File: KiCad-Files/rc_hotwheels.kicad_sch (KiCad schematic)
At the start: 9 parts, among them IC1 BD6211F-E2, IC2 MIC5504-3.3YM5-TR, U1 STM32F070F6P6, U3 NRF24L01_Breakout

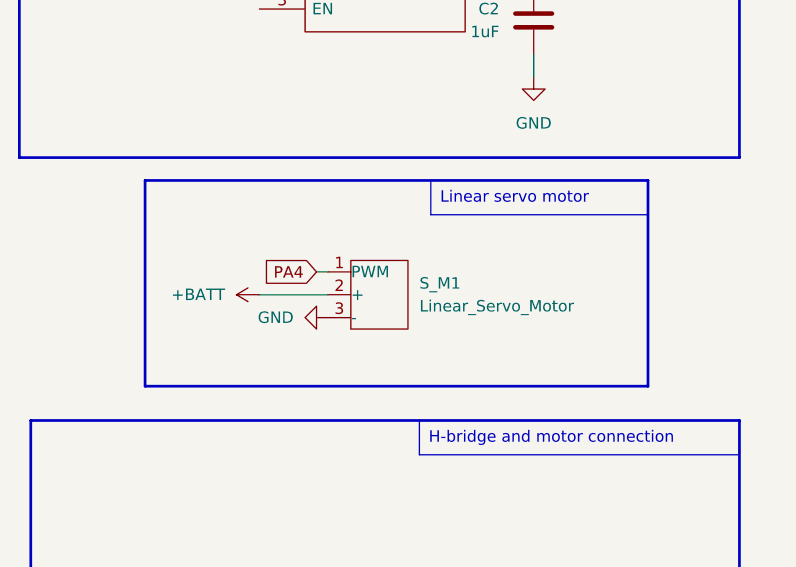
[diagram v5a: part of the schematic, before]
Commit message: Servo motor connection
Deleted unused component - servo motor, instead used mounting holes
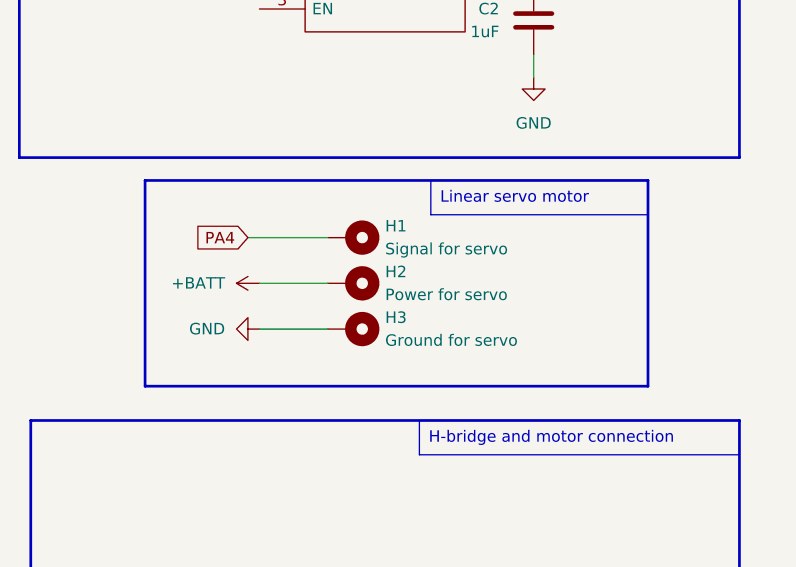
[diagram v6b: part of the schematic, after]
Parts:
- removed S_M1: Linear_Servo_Motor, symbol Motor:Motor_Servo
- added H1: Signal for servo, symbol Mechanical:MountingHole_Pad
- added H2: Power for servo, symbol Mechanical:MountingHole_Pad
- added H3: Ground for servo, symbol Mechanical:MountingHole_Pad
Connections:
- net +BATT: now also H2.1
- net GND: now also H3.1
- net PA4: now also H1.1
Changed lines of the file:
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@@
+    (stroke (width 0) (type default))
+  )
+  (wire (pts (xy 41.91 128.27) (xy 49.53 128.27))
     (stroke (width 0) (type default))
   )
@@
     (stroke (width 0) (type default))
   )
-  (wire (pts (xy 41.91 124.46) (xy 49.53 124.46))
+  (wire (pts (xy 41.91 123.19) (xy 49.53 123.19))
     (stroke (width 0) (type default))
   )
@@
     (stroke (width 0) (type default))
   )
-  (wire (pts (xy 48.26 121.92) (xy 49.53 121.92))
+  (wire (pts (xy 40.64 118.11) (xy 49.53 118.11))
     (stroke (width 0) (type default))
   )
@@
     )
   )
-  (global_label "PA4" (shape input) (at 48.26 121.92 180) (fields_autoplaced)
-    (effects (font (size 1.27 1.27)) (justify right))
-    (property "Intersheetrefs" "${INTERSHEET_REFS}" (at 41.7067 121.92 0)
-      (effects (font (size 1.27 1.27)) (justify right) hide)
-    )
-    (property "Servo Control" "" (at 48.26 124.1108 0)
+  (global_label "PA4" (shape input) (at 40.64 118.11 180) (fields_autoplaced)
+    (effects (font (size 1.27 1.27)) (justify right))
+    (property "Intersheetrefs" "${INTERSHEET_REFS}" (at 34.0867 118.11 0)
+      (effects (font (size 1.27 1.27)) (justify right) hide)
+    )
+    (property "Servo Control" "" (at 40.64 120.3008 0)
       (effects (font (size 1.27 1.27)) (justify right) hide)
     )
@@
     (property "Intersheetrefs" "${INTERSHEET_REFS}" (at 87.41 90.17 0)
       (effects (font (size 1.27 1.27)) (justify left) hide)
+    )
+  )
+  (symbol (lib_id "Mechanical:MountingHole_Pad") (at 52.07 118.11 270) (unit 1)
+    (in_bom yes) (on_board yes) (dnp no) (fields_autoplaced)
+    (property "Reference" "H1" (at 55.88 116.84 90)
+      (effects (font (size 1.27 1.27)) (justify left))
+    )
+    (property "Value" "Signal for servo" (at 55.88 119.38 90)
+      (effects (font (size 1.27 1.27)) (justify left))
+    )
+    (property "Footprint" "" (at 52.07 118.11 0)
+      (effects (font (size 1.27 1.27)) hide)
+    )
+    (property "Datasheet" "~" (at 52.07 118.11 0)
+      (effects (font (size 1.27 1.27)) hide)
+    )
+    (pin "1")
+    (instances
+      (project "rc_hotwheels"
+        (path "/0b835094-f9c0-45ab-a312-d1f27d043c8e"
+          (reference "H1") (unit 1)
+        )
+      )
     )
   )
@@
         (path "/0b835094-f9c0-45ab-a312-d1f27d043c8e"
           (reference "#PWR06") (unit 1)
+        )
+      )
+    )
+  )
+  (symbol (lib_id "Mechanical:MountingHole_Pad") (at 52.07 128.27 270) (unit 1)
+    (in_bom yes) (on_board yes) (dnp no) (fields_autoplaced)
+    (property "Reference" "H3" (at 55.88 127 90)
+      (effects (font (size 1.27 1.27)) (justify left))
+    )
+    (property "Value" "Ground for servo" (at 55.88 129.54 90)
+      (effects (font (size 1.27 1.27)) (justify left))
+    )
+    (property "Footprint" "" (at 52.07 128.27 0)
+      (effects (font (size 1.27 1.27)) hide)
+    )
+    (property "Datasheet" "~" (at 52.07 128.27 0)
+      (effects (font (size 1.27 1.27)) hide)
+    )
+    (pin "1")
+    (instances
+      (project "rc_hotwheels"
+        (path "/0b835094-f9c0-45ab-a312-d1f27d043c8e"
+          (reference "H3") (unit 1)
         )
       )
@@
     )
   )
-  (symbol (lib_id "power:+BATT") (at 41.91 124.46 90) (unit 1)
+  (symbol (lib_id "power:+BATT") (at 41.91 123.19 90) (unit 1)
     (in_bom yes) (on_board yes) (dnp no)
-    (property "Reference" "#PWR03" (at 45.72 124.46 0)
-      (effects (font (size 1.27 1.27)) hide)
-    )
-    (property "Value" "+BATT" (at 38.1 124.46 90)
-      (effects (font (size 1.27 1.27)) (justify left))
-    )
-    (property "Footprint" "" (at 41.91 124.46 0)
-      (effects (font (size 1.27 1.27)) hide)
-    )
-    (property "Datasheet" "" (at 41.91 124.46 0)
+    (property "Reference" "#PWR03" (at 45.72 123.19 0)
+      (effects (font (size 1.27 1.27)) hide)
+    )
+    (property "Value" "+BATT" (at 38.1 123.19 90)
+      (effects (font (size 1.27 1.27)) (justify left))
+    )
+    (property "Footprint" "" (at 41.91 123.19 0)
+      (effects (font (size 1.27 1.27)) hide)
+    )
+    (property "Datasheet" "" (at 41.91 123.19 0)
       (effects (font (size 1.27 1.27)) hide)
     )
@@
     )
   )
+  (symbol (lib_id "Mechanical:MountingHole_Pad") (at 52.07 123.19 270) (unit 1)
+    (in_bom yes) (on_board yes) (dnp no) (fields_autoplaced)
+    (property "Reference" "H2" (at 55.88 121.92 90)
+      (effects (font (size 1.27 1.27)) (justify left))
+    )
+    (property "Value" "Power for servo" (at 55.88 124.46 90)
+      (effects (font (size 1.27 1.27)) (justify left))
+    )
+    (property "Footprint" "" (at 52.07 123.19 0)
+      (effects (font (size 1.27 1.27)) hide)
+    )
+    (property "Datasheet" "~" (at 52.07 123.19 0)
+      (effects (font (size 1.27 1.27)) hide)
+    )
+    (pin "1")
+    (instances
+      (project "rc_hotwheels"
+        (path "/0b835094-f9c0-45ab-a312-d1f27d043c8e"
+          (reference "H2") (unit 1)
+        )
+      )
+    )
+  )
   (symbol (lib_id "power:GND") (at 73.66 57.15 0) (unit 1)
     (in_bom yes) (on_board yes) (dnp no) (fields_autoplaced)
@@
     )
   )
-  (symbol (lib_id "power:GND") (at 49.53 127 270) (unit 1)
-    (in_bom yes) (on_board yes) (dnp no) (fields_autoplaced)
-    (property "Reference" "#PWR08" (at 43.18 127 0)
-      (effects (font (size 1.27 1.27)) hide)
-    )
-    (property "Value" "GND" (at 45.72 127 90)
-      (effects (font (size 1.27 1.27)) (justify right))
-    )
-    (property "Footprint" "" (at 49.53 127 0)
-      (effects (font (size 1.27 1.27)) hide)
-    )
-    (property "Datasheet" "" (at 49.53 127 0)
+  (symbol (lib_id "power:GND") (at 41.91 128.27 270) (unit 1)
+    (in_bom yes) (on_board yes) (dnp no) (fields_autoplaced)
+    (property "Reference" "#PWR08" (at 35.56 128.27 0)
+      (effects (font (size 1.27 1.27)) hide)
+    )
+    (property "Value" "GND" (at 38.1 128.27 90)
+      (effects (font (size 1.27 1.27)) (justify right))
+    )
+    (property "Footprint" "" (at 41.91 128.27 0)
+      (effects (font (size 1.27 1.27)) hide)
+    )
+    (property "Datasheet" "" (at 41.91 128.27 0)
       (effects (font (size 1.27 1.27)) hide)
     )
@@
         )
       )
-    )
-  )
-  (symbol (lib_id "Motor:Motor_Servo") (at 57.15 125.73 0) (unit 1)
-    (in_bom yes) (on_board yes) (dnp no) (fields_autoplaced)
-    (property "Reference" "S_M1" (at 59.69 123.19 0)
-      (effects (font (size 1.27 1.27)) (justify left))
-    )
-    (property "Value" "Linear_Servo_Motor" (at 59.69 125.73 0)
-      (effects (font (size 1.27 1.27)) (justify left))
-    )
-    (property "Footprint" "" (at 57.15 129.286 0)
-      (effects (font (size 1.27 1.27)) hide)
-    )
-    (property "Datasheet" "" (at 57.15 129.286 0)
-      (effects (font (size 1.27 1.27)) hide)
-    )
-    (pin "1")
-    (pin "2")
-    (pin "3")
-    (instances
-      (project "rc_hotwheels"
-        (path "/0b835094-f9c0-45ab-a312-d1f27d043c8e"
-          (reference "S_M1") (unit 1)
-        )
-      )

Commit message: Mounting holes footprints added
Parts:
- H1, H2, H3: footprint (none) -> MountingHole:MountingHole_2.2mm_M2_DIN965_Pad
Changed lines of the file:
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@@
       (effects (font (size 1.27 1.27)) (justify left))
     )
-    (property "Footprint" "" (at 52.07 118.11 0)
+    (property "Footprint" "MountingHole:MountingHole_2.2mm_M2_DIN965_Pad" (at 52.07 118.11 0)
       (effects (font (size 1.27 1.27)) hide)
     )
@@
       (effects (font (size 1.27 1.27)) (justify left))
     )
-    (property "Footprint" "" (at 52.07 128.27 0)
+    (property "Footprint" "MountingHole:MountingHole_2.2mm_M2_DIN965_Pad" (at 52.07 128.27 0)
       (effects (font (size 1.27 1.27)) hide)
     )
@@
       (effects (font (size 1.27 1.27)) (justify left))
     )
-    (property "Footprint" "" (at 52.07 123.19 0)
-      (effects (font (size 1.27 1.27)) hide)
-    )
+    (property "Footprint" "MountingHole:MountingHole_2.2mm_M2_DIN965_Pad" (at 52.07 123.19 0)
+      (effects (font (size 1.27 1.27)) hide)
+    )

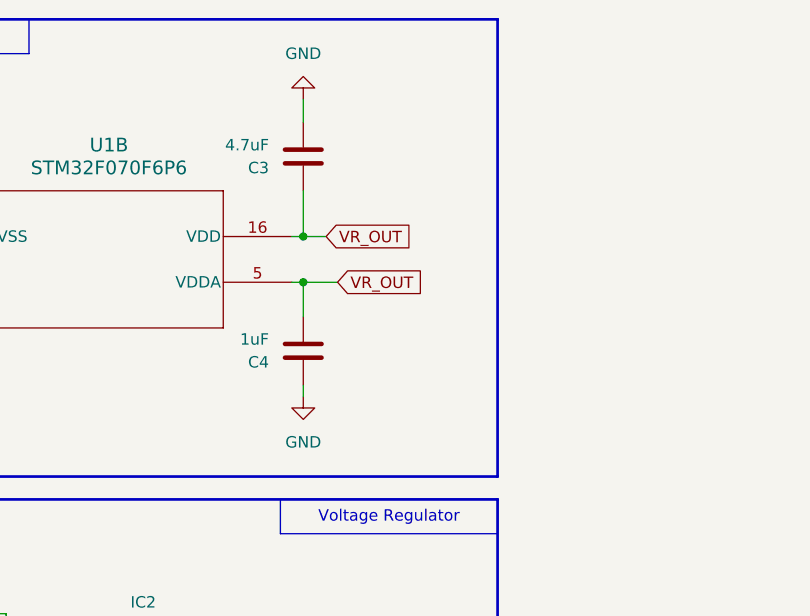
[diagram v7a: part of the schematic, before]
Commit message: Added more capacitors for power supply of MCU
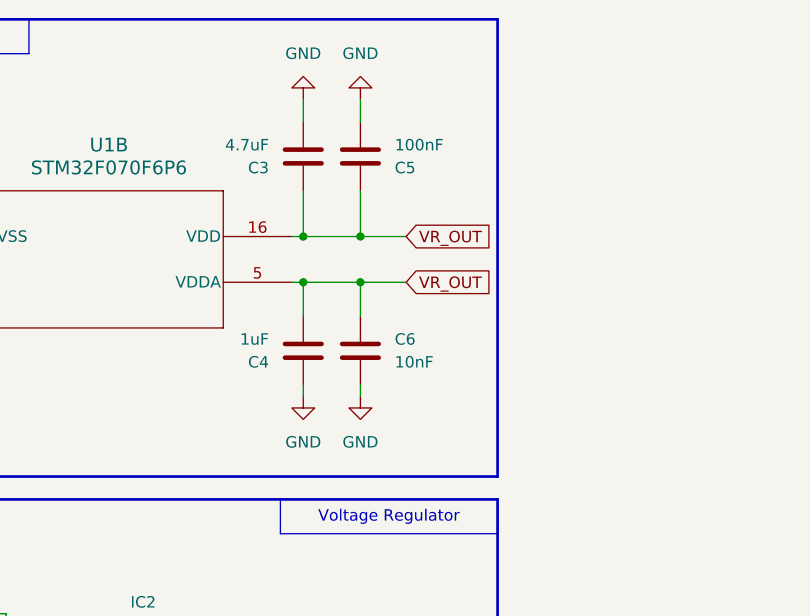
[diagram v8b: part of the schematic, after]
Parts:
- added C5: 100nF, Capacitor_THT:C_Rect_L4.6mm_W2.0mm_P2.50mm_MKS02_FKP02, symbol Device:C
- added C6: 10nF, Capacitor_THT:C_Rect_L4.6mm_W2.0mm_P2.50mm_MKS02_FKP02, symbol Device:C
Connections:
- net GND: now also C5.1, C6.1
- net VR_OUT: now also C5.2, C6.2
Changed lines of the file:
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@@
   (junction (at 229.87 139.7) (diameter 0) (color 0 0 0 0)
   )
+  (junction (at 80.01 39.37) (diameter 0) (color 0 0 0 0)
+  )
+  (junction (at 80.01 44.45) (diameter 0) (color 0 0 0 0)
+  )
   (junction (at 72.39 90.17) (diameter 0) (color 0 0 0 0)
   )
@@
     (stroke (width 0) (type default))
   )
+  (wire (pts (xy 80.01 44.45) (xy 80.01 48.26))
+    (stroke (width 0) (type default))
+  )
   (wire (pts (xy 41.91 128.27) (xy 49.53 128.27))
     (stroke (width 0) (type default))
@@
     (stroke (width 0) (type default))
   )
+  (wire (pts (xy 80.01 44.45) (xy 85.09 44.45))
+    (stroke (width 0) (type default))
+  )
   (wire (pts (xy 229.87 139.7) (xy 229.87 148.59))
     (stroke (width 0) (type default))
@@
     (stroke (width 0) (type default))
   )
+  (wire (pts (xy 80.01 34.29) (xy 80.01 39.37))
+    (stroke (width 0) (type default))
+  )
   (wire (pts (xy 41.91 176.53) (xy 41.91 175.26))
     (stroke (width 0) (type default))
@@
     (stroke (width 0) (type default))
   )
+  (wire (pts (xy 80.01 24.13) (xy 80.01 26.67))
+    (stroke (width 0) (type default))
+  )
   (wire (pts (xy 30.48 81.28) (xy 36.83 81.28))
     (stroke (width 0) (type default))
@@
     (stroke (width 0) (type default))
   )
+  (wire (pts (xy 80.01 39.37) (xy 85.09 39.37))
+    (stroke (width 0) (type default))
+  )
   (wire (pts (xy 233.68 135.89) (xy 229.87 135.89))
     (stroke (width 0) (type default))
@@
     (stroke (width 0) (type default))
   )
-  (wire (pts (xy 73.66 44.45) (xy 77.47 44.45))
+  (wire (pts (xy 73.66 44.45) (xy 80.01 44.45))
     (stroke (width 0) (type default))
   )
@@
     (stroke (width 0) (type default))
   )
-  (wire (pts (xy 73.66 39.37) (xy 76.2 39.37))
+  (wire (pts (xy 73.66 39.37) (xy 80.01 39.37))
     (stroke (width 0) (type default))
   )
   (wire (pts (xy 234.95 148.59) (xy 246.38 148.59))
+    (stroke (width 0) (type default))
+  )
+  (wire (pts (xy 80.01 57.15) (xy 80.01 55.88))
     (stroke (width 0) (type default))
   )
@@
     )
   )
-  (global_label "VR_OUT" (shape input) (at 76.2 39.37 0) (fields_autoplaced)
+  (global_label "VR_OUT" (shape input) (at 85.09 39.37 0) (fields_autoplaced)
     (effects (font (size 1.27 1.27)) (justify left))
-    (property "Intersheetrefs" "${INTERSHEET_REFS}" (at 86.14 39.37 0)
+    (property "Intersheetrefs" "${INTERSHEET_REFS}" (at 95.03 39.37 0)
       (effects (font (size 1.27 1.27)) (justify left) hide)
     )
@@
     )
   )
-  (global_label "VR_OUT" (shape input) (at 77.47 44.45 0) (fields_autoplaced)
+  (global_label "VR_OUT" (shape input) (at 85.09 44.45 0) (fields_autoplaced)
     (effects (font (size 1.27 1.27)) (justify left))
-    (property "Intersheetrefs" "${INTERSHEET_REFS}" (at 87.41 44.45 0)
+    (property "Intersheetrefs" "${INTERSHEET_REFS}" (at 95.03 44.45 0)
       (effects (font (size 1.27 1.27)) (justify left) hide)
     )
@@
     )
   )
+  (symbol (lib_id "power:GND") (at 80.01 57.15 0) (unit 1)
+    (in_bom yes) (on_board yes) (dnp no) (fields_autoplaced)
+    (property "Reference" "#PWR010" (at 80.01 63.5 0)
+      (effects (font (size 1.27 1.27)) hide)
+    )
+    (property "Value" "GND" (at 80.01 62.23 0)
+      (effects (font (size 1.27 1.27)))
+    )
+    (property "Footprint" "" (at 80.01 57.15 0)
+      (effects (font (size 1.27 1.27)) hide)
+    )
+    (property "Datasheet" "" (at 80.01 57.15 0)
+      (effects (font (size 1.27 1.27)) hide)
+    )
+    (pin "1")
+    (instances
+      (project "rc_hotwheels"
+        (path "/0b835094-f9c0-45ab-a312-d1f27d043c8e"
+          (reference "#PWR010") (unit 1)
+        )
+      )
+    )
+  )
   (symbol (lib_id "power:GND") (at 73.66 24.13 180) (unit 1)
     (in_bom yes) (on_board yes) (dnp no) (fields_autoplaced)
@@
         (path "/0b835094-f9c0-45ab-a312-d1f27d043c8e"
           (reference "C1") (unit 1)
+        )
+      )
+    )
+  )
+  (symbol (lib_id "power:GND") (at 80.01 24.13 0) (mirror x) (unit 1)
+    (in_bom yes) (on_board yes) (dnp no) (fields_autoplaced)
+    (property "Reference" "#PWR09" (at 80.01 17.78 0)
+      (effects (font (size 1.27 1.27)) hide)
+    )
+    (property "Value" "GND" (at 80.01 19.05 0)
+      (effects (font (size 1.27 1.27)))
+    )
+    (property "Footprint" "" (at 80.01 24.13 0)
+      (effects (font (size 1.27 1.27)) hide)
+    )
+    (property "Datasheet" "" (at 80.01 24.13 0)
+      (effects (font (size 1.27 1.27)) hide)
+    )
+    (pin "1")
+    (instances
+      (project "rc_hotwheels"
+        (path "/0b835094-f9c0-45ab-a312-d1f27d043c8e"
+          (reference "#PWR09") (unit 1)
+        )
+      )
+    )
+  )
+  (symbol (lib_id "Device:C") (at 80.01 52.07 180) (unit 1)
+    (in_bom yes) (on_board yes) (dnp no)
+    (property "Reference" "C6" (at 83.82 50.8 0)
+      (effects (font (size 1.27 1.27)) (justify right))
+    )
+    (property "Value" "10nF" (at 83.82 53.34 0)
+      (effects (font (size 1.27 1.27)) (justify right))
+    )
+    (property "Footprint" "Capacitor_THT:C_Rect_L4.6mm_W2.0mm_P2.50mm_MKS02_FKP02" (at 79.0448 48.26 0)
+      (effects (font (size 1.27 1.27)) hide)
+    )
+    (property "Datasheet" "~" (at 80.01 52.07 0)
+      (effects (font (size 1.27 1.27)) hide)
+    )
+    (pin "1")
+    (pin "2")
+    (instances
+      (project "rc_hotwheels"
+        (path "/0b835094-f9c0-45ab-a312-d1f27d043c8e"
+          (reference "C6") (unit 1)
         )
       )
@@
         )
       )
+    )
+  )
+  (symbol (lib_id "Device:C") (at 80.01 30.48 0) (mirror y) (unit 1)
+    (in_bom yes) (on_board yes) (dnp no)
+    (property "Reference" "C5" (at 83.82 31.75 0)
+      (effects (font (size 1.27 1.27)) (justify right))
+    )
+    (property "Value" "100nF" (at 83.82 29.21 0)
+      (effects (font (size 1.27 1.27)) (justify right))
+    )
+    (property "Footprint" "Capacitor_THT:C_Rect_L4.6mm_W2.0mm_P2.50mm_MKS02_FKP02" (at 79.0448 34.29 0)
+      (effects (font (size 1.27 1.27)) hide)
+    )
+    (property "Datasheet" "~" (at 80.01 30.48 0)
+      (effects (font (size 1.27 1.27)) hide)
+    )
+    (pin "1")
+    (pin "2")
+    (instances
+      (project "rc_hotwheels"
+        (path "/0b835094-f9c0-45ab-a312-d1f27d043c8e"
+          (reference "C5") (unit 1)
+        )
+      )
